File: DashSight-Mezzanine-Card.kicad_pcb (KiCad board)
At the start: 2 copper layers, 72 x 78.5 mm, 70 parts, among them IC1 XM1110, IC2 ELM327, J1 Pi2 Connector, J2 Euler Connector, J3 Conn_Coaxial, J4 OBD2-DB9_Male, Q1 2N3904, Q2 2N3906, Q3 2N3906, Q4 2N3904, Q5 2N3904, Q6 2N3904, Q7 2N3904, U1 MCP2561-E/P, U2 LM317L_TO92, U3 LM1085-5.0, U4 ADuM1201AR, Y1 4.0MHz

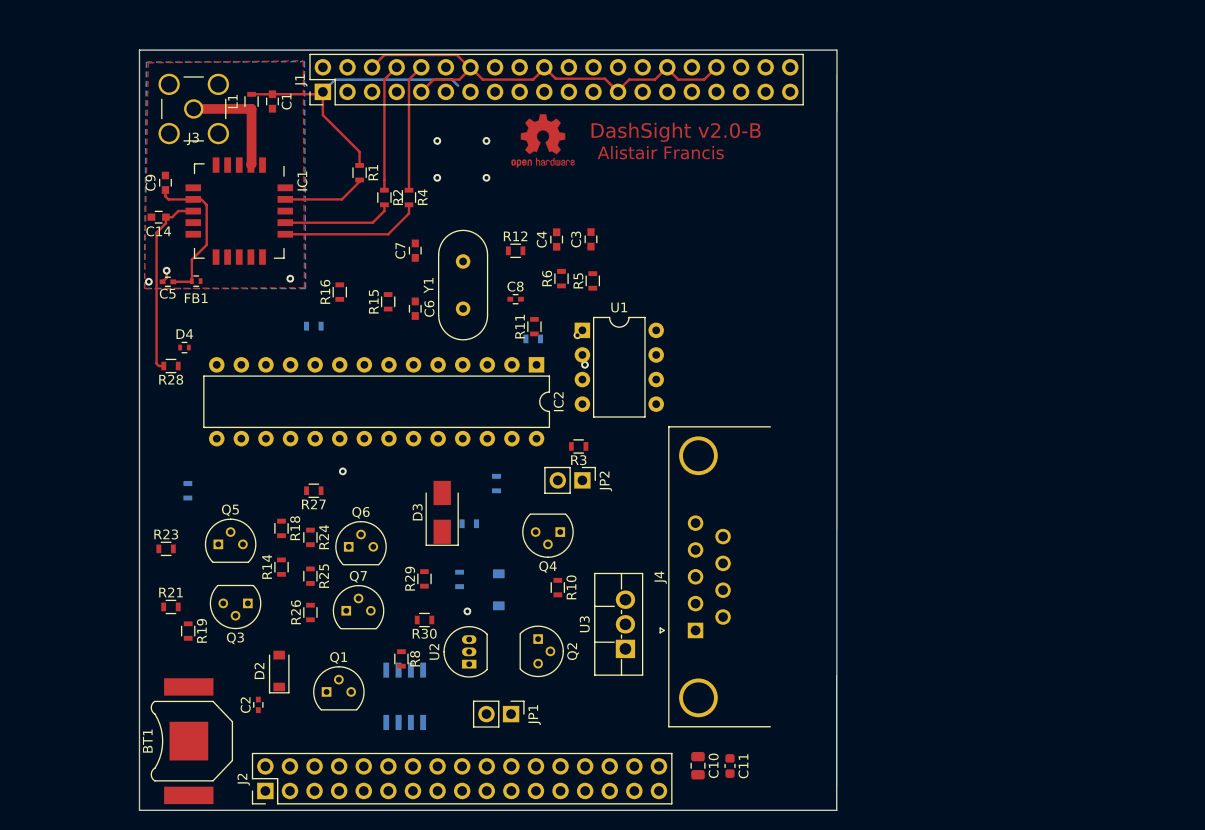
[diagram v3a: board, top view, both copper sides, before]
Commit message: pcb: Upgrade to 4 layers and start to prep GNSS
Signed-off-by: Alistair Francis <alistair@alistair23.me>
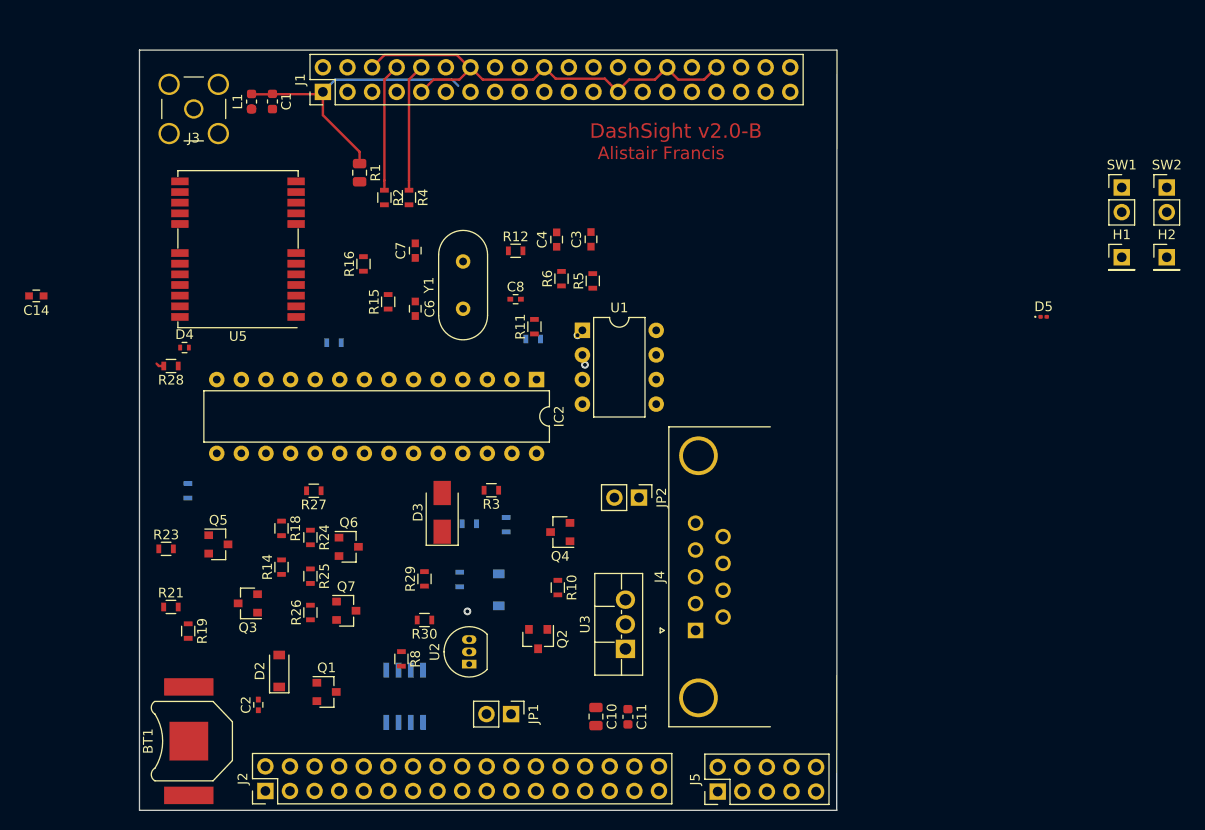
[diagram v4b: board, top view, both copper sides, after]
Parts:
- removed C5: 0.1uF, Capacitors_SMD:C_0402
- removed C9: 1uF, Capacitors_SMD:C_0603
- removed FB1: 600Ohm/100MHz, Inductors_SMD:L_0402
- removed IC1: XM1110, RF_GPS:Sierra_XM11X0
- removed REF***: OSHW-Logo2_7.3x6mm_Copper, Symbols:OSHW-Logo2_7.3x6mm_Copper
- added D5: D_Zener, Diode_SMD:D_0201_0603Metric, F.Cu at (221.4, 74.0)
- added H1: Safeboot, Connector_PinHeader_2.54mm:PinHeader_1x01_P2.54mm_Vertical, F.Cu at (229.4, 67.9)
- added H2: Reset, Connector_PinHeader_2.54mm:PinHeader_1x01_P2.54mm_Vertical, F.Cu at (234.1, 67.9)
- added J5: Conn_02x05_Odd_Even, Connector_PinHeader_2.54mm:PinHeader_2x05_P2.54mm_Vertical, F.Cu at (187.7, 123.1)
- added SW1: SW_Push, Connector_PinHeader_2.54mm:PinHeader_1x02_P2.54mm_Vertical, F.Cu at (229.4, 60.7)
- added SW2: SW_Push, Connector_PinHeader_2.54mm:PinHeader_1x02_P2.54mm_Vertical, F.Cu at (234.1, 60.7)
- added U5: NEO-M9N, RF_GPS:ublox_NEO, F.Cu at (138.2, 67.1)
- C1: value 1uF -> 47pF; footprint Capacitors_SMD:C_0603 -> Capacitor_SMD:C_0603_1608Metric
- L1: value 33nH -> 30Ohm/1.8A; footprint Inductors_SMD:L_0603 -> Inductor_SMD:L_0603_1608Metric
- Q1, Q2, Q3, Q4, Q5, Q6, Q7: footprint TO_SOT_Packages_THT:TO-92_Molded_Narrow -> Package_TO_SOT_SMD:SOT-23
- R1: value 10K -> 10; footprint Resistors_SMD:R_0603 -> Resistor_SMD:R_0805_2012Metric
- moved C14 15.0 mm to (117.3, 71.9)
- moved C10 11.7 mm to (175.1, 115.3)
- moved C11 11.7 mm to (178.4, 115.3)
- moved R3 10.1 mm to (164.3, 91.9)
- moved JP2 6.11 mm to (179.6, 92.7)
- moved R13 4.36 mm to (165.9, 95.5)
- moved R16 3.80 mm to (151.1, 68.6)
- moved R22 2.69 mm to (148.1, 76.7)
- moved IC2 1.52 mm to (169.0, 80.5)
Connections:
- C1 pad 1: +3V3 -> Net-(C1-Pad1)
- IC2 pad 25: Net-(IC2-Pad25) -> (no net)
- IC2 pad 26: Net-(IC2-Pad26) -> (no net)
- IC2 pad 27: Net-(IC2-Pad27) -> (no net)
- IC2 pad 28: Net-(IC2-Pad28) -> (no net)
- J1 pad 11: Net-(J1-Pad11) -> (no net)
- J1 pad 12: Net-(J1-Pad12) -> (no net)
- J1 pad 13: Net-(J1-Pad13) -> (no net)
- J1 pad 15: Net-(J1-Pad15) -> (no net)
- J1 pad 16: Net-(J1-Pad16) -> (no net)
- J1 pad 17: Net-(J1-Pad17) -> (no net)
- J1 pad 18: Net-(J1-Pad18) -> (no net)
- J1 pad 19: Net-(J1-Pad19) -> (no net)
- J1 pad 2: Net-(J1-Pad2) -> (no net)
- J1 pad 21: Net-(J1-Pad21) -> (no net)
- J1 pad 22: Net-(J1-Pad22) -> (no net)
- J1 pad 23: Net-(J1-Pad23) -> (no net)
- J1 pad 24: Net-(J1-Pad24) -> (no net)
- J1 pad 26: Net-(J1-Pad26) -> (no net)
- J1 pad 27: Net-(J1-Pad27) -> (no net)
- J1 pad 28: Net-(J1-Pad28) -> (no net)
- J1 pad 29: Net-(J1-Pad29) -> (no net)
- J1 pad 3: Net-(J1-Pad3) -> (no net)
- J1 pad 31: Net-(J1-Pad31) -> (no net)
- J1 pad 32: Net-(J1-Pad32) -> (no net)
- J1 pad 33: Net-(J1-Pad33) -> (no net)
- J1 pad 35: Net-(J1-Pad35) -> (no net)
- J1 pad 36: Net-(J1-Pad36) -> (no net)
- J1 pad 37: Net-(J1-Pad37) -> (no net)
- J1 pad 38: Net-(J1-Pad38) -> (no net)
- J1 pad 4: Net-(J1-Pad4) -> (no net)
- J1 pad 40: Net-(J1-Pad40) -> (no net)
- J1 pad 5: Net-(J1-Pad5) -> (no net)
- J1 pad 7: Net-(J1-Pad7) -> (no net)
- J2 pad 1: Net-(J2-Pad1) -> (no net)
- J2 pad 10: Net-(J2-Pad10) -> (no net)
- J2 pad 11: Net-(J2-Pad11) -> (no net)
- J2 pad 12: Net-(J2-Pad12) -> (no net)
- J2 pad 13: Net-(J2-Pad13) -> (no net)
- J2 pad 15: Net-(J2-Pad15) -> (no net)
- J2 pad 16: Net-(J2-Pad16) -> (no net)
- J2 pad 17: Net-(J2-Pad17) -> (no net)
- J2 pad 18: Net-(J2-Pad18) -> (no net)
- J2 pad 19: Net-(J2-Pad19) -> (no net)
- J2 pad 21: Net-(J2-Pad21) -> (no net)
- J2 pad 22: Net-(J2-Pad22) -> (no net)
- J2 pad 26: Net-(J2-Pad26) -> (no net)
- J2 pad 27: Net-(J2-Pad27) -> (no net)
- J2 pad 28: Net-(J2-Pad28) -> (no net)
- J2 pad 29: Net-(J2-Pad29) -> (no net)
- J2 pad 3: Net-(J2-Pad3) -> (no net)
- J2 pad 30: Net-(J2-Pad30) -> (no net)
- J2 pad 31: Net-(J2-Pad31) -> (no net)
- J2 pad 32: Net-(J2-Pad32) -> (no net)
- J2 pad 33: Net-(J2-Pad33) -> (no net)
- J2 pad 5: Net-(J2-Pad5) -> (no net)
- J2 pad 7: Net-(J2-Pad7) -> (no net)
- J2 pad 8: Net-(J2-Pad8) -> (no net)
- L1 pad 2: +3V3 -> Net-(C1-Pad1)
- R1 pad 1: +3V3 -> Net-(C1-Pad1)
- R2 pad 1: UART2_TX -> Net-(R2-Pad1)
- R2 pad 2: Net-(IC1-Pad17) -> UART2_TX
- R4 pad 1: UART2_RX -> Net-(R4-Pad1)
- R4 pad 2: Net-(IC1-Pad16) -> UART2_RX
- U1 pad 5: Net-(U1-Pad5) -> (no net)
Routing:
- net Net-(BT1-Pad1): track 19.5 -> 0.84 mm
- net Net-(C5-Pad1): track 16.7 -> 0.00 mm
- net Net-(IC1-Pad16): track 14.6 -> 0.00 mm
- net Net-(D5-Pad1): track 11.8 -> 0.02 mm
- net Net-(IC1-Pad17): track 11.4 -> 0.00 mm
- net Net-(R1-Pad2): track 8.62 -> 0.18 mm
- net GND: track 48.7 -> 47.3 mm, vias 7 -> 0
- net ELM_Pin12: vias 1 -> 0
- removed copper zone on B.Cu, net GND
- removed copper zone on F.Cu, net GND
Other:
- copper layers 2 -> 4

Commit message: pcb: Add ground and power planes on inner layers
Signed-off-by: Alistair Francis <alistair@alistair23.me>
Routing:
- added copper zone on In2.Cu, net +3V3
- added copper zone on In1.Cu, net GND
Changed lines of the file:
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@@
     (add_net "Net-(IC2-Pad21)")
     (add_net "Net-(IC2-Pad22)")
-    (add_net "Net-(IC2-Pad25)")
-    (add_net "Net-(IC2-Pad26)")
-    (add_net "Net-(IC2-Pad27)")
-    (add_net "Net-(IC2-Pad28)")
     (add_net "Net-(IC2-Pad3)")
     (add_net "Net-(IC2-Pad4)")
-    (add_net "Net-(J1-Pad11)")
-    (add_net "Net-(J1-Pad12)")
-    (add_net "Net-(J1-Pad13)")
-    (add_net "Net-(J1-Pad15)")
-    (add_net "Net-(J1-Pad16)")
-    (add_net "Net-(J1-Pad17)")
-    (add_net "Net-(J1-Pad18)")
-    (add_net "Net-(J1-Pad19)")
-    (add_net "Net-(J1-Pad2)")
-    (add_net "Net-(J1-Pad21)")
-    (add_net "Net-(J1-Pad22)")
-    (add_net "Net-(J1-Pad23)")
-    (add_net "Net-(J1-Pad24)")
-    (add_net "Net-(J1-Pad26)")
-    (add_net "Net-(J1-Pad27)")
-    (add_net "Net-(J1-Pad28)")
-    (add_net "Net-(J1-Pad29)")
-    (add_net "Net-(J1-Pad3)")
-    (add_net "Net-(J1-Pad31)")
-    (add_net "Net-(J1-Pad32)")
-    (add_net "Net-(J1-Pad33)")
-    (add_net "Net-(J1-Pad35)")
-    (add_net "Net-(J1-Pad36)")
-    (add_net "Net-(J1-Pad37)")
-    (add_net "Net-(J1-Pad38)")
-    (add_net "Net-(J1-Pad4)")
-    (add_net "Net-(J1-Pad40)")
-    (add_net "Net-(J1-Pad5)")
-    (add_net "Net-(J1-Pad7)")
-    (add_net "Net-(J2-Pad1)")
-    (add_net "Net-(J2-Pad10)")
-    (add_net "Net-(J2-Pad11)")
-    (add_net "Net-(J2-Pad12)")
-    (add_net "Net-(J2-Pad13)")
-    (add_net "Net-(J2-Pad15)")
-    (add_net "Net-(J2-Pad16)")
-    (add_net "Net-(J2-Pad17)")
-    (add_net "Net-(J2-Pad18)")
-    (add_net "Net-(J2-Pad19)")
-    (add_net "Net-(J2-Pad21)")
-    (add_net "Net-(J2-Pad22)")
-    (add_net "Net-(J2-Pad26)")
-    (add_net "Net-(J2-Pad27)")
-    (add_net "Net-(J2-Pad28)")
-    (add_net "Net-(J2-Pad29)")
-    (add_net "Net-(J2-Pad3)")
-    (add_net "Net-(J2-Pad30)")
-    (add_net "Net-(J2-Pad31)")
-    (add_net "Net-(J2-Pad32)")
-    (add_net "Net-(J2-Pad33)")
-    (add_net "Net-(J2-Pad5)")
-    (add_net "Net-(J2-Pad7)")
-    (add_net "Net-(J2-Pad8)")
-    (add_net "Net-(J5-Pad10)")
-    (add_net "Net-(J5-Pad2)")
-    (add_net "Net-(J5-Pad3)")
-    (add_net "Net-(J5-Pad7)")
-    (add_net "Net-(J5-Pad8)")
     (add_net "Net-(Q1-Pad2)")
     (add_net "Net-(Q2-Pad1)")
@@
     (add_net "Net-(R3-Pad1)")
     (add_net "Net-(R4-Pad1)")
-    (add_net "Net-(U1-Pad5)")
-    (add_net "Net-(U5-Pad14)")
-    (add_net "Net-(U5-Pad15)")
-    (add_net "Net-(U5-Pad16)")
-    (add_net "Net-(U5-Pad17)")
-    (add_net "Net-(U5-Pad18)")
-    (add_net "Net-(U5-Pad19)")
-    (add_net "Net-(U5-Pad3)")
-    (add_net "Net-(U5-Pad4)")
-    (add_net "Net-(U5-Pad5)")
-    (add_net "Net-(U5-Pad6)")
     (add_net PowerOn)
     (add_net PwrCntrl)
-    (add_net ResetSW)
     (add_net UART2_RX)
     (add_net UART2_TX)
@@
   (segment (start 155.829 59.956) (end 155.829 49.53) (width 0.25) (layer F.Cu) (net 19))
   (segment (start 155.829 60.972) (end 155.829 59.956) (width 0.25) (layer F.Cu) (net 19))
+  (segment (start 155.829 62.472) (end 155.829 62.484) (width 0.25) (layer F.Cu) (net 19) (status 30))
   (via (at 174 79) (size 0.8) (drill 0.4) (layers F.Cu B.Cu) (net 27))
   (segment (start 160.909 50.181) (end 160.274 49.546) (width 0.25) (layer B.Cu) (net 35))
@@
   (segment (start 153.289 60.972) (end 153.289 59.956) (width 0.25) (layer F.Cu) (net 38))
   (via (at 173.228 75.946) (size 0.8) (drill 0.4) (layers F.Cu B.Cu) (net 42))
-  (segment (start 155.829 62.472) (end 155.829 62.484) (width 0.25) (layer F.Cu) (net 19) (status 30))
-  (segment (start 150.731 59.909) (end 150.731 60.089) (width 0.25) (layer F.Cu) (net 57) (status 30))
   (segment (start 129.761999 78.878499) (end 130.0045 79.121) (width 0.25) (layer F.Cu) (net 45))
   (segment (start 130.0045 79.121) (end 130.5045 79.121) (width 0.25) (layer F.Cu) (net 45))
   (segment (start 139.561 52.578) (end 139.573 52.566) (width 1) (layer F.Cu) (net 53))
+  (segment (start 150.731 59.909) (end 150.731 60.089) (width 0.25) (layer F.Cu) (net 57) (status 30))
+  (zone (net 1) (net_name GND) (layer In1.Cu) (hatch edge 0.508)
+    (connect_pads (clearance 0.508))
+    (min_thickness 0.254)
+    (fill yes (arc_segments 32) (thermal_gap 0.508) (thermal_bridge_width 0.508))
+    (polygon
+      (pts
+        (xy 199.39 123.825) (xy 128.905 123.825) (xy 128.905 47.625) (xy 199.39 47.625)
+      )
+    )
+  )
+  (zone (net 35) (net_name +3V3) (layer In2.Cu) (hatch edge 0.508)
+    (connect_pads (clearance 0.508))
+    (min_thickness 0.254)
+    (fill yes (arc_segments 32) (thermal_gap 0.508) (thermal_bridge_width 0.508))
+    (polygon
+      (pts
+        (xy 196.85 118.11) (xy 130.81 118.11) (xy 130.81 53.34) (xy 196.85 53.34)
+      )
+    )
+  )
 )

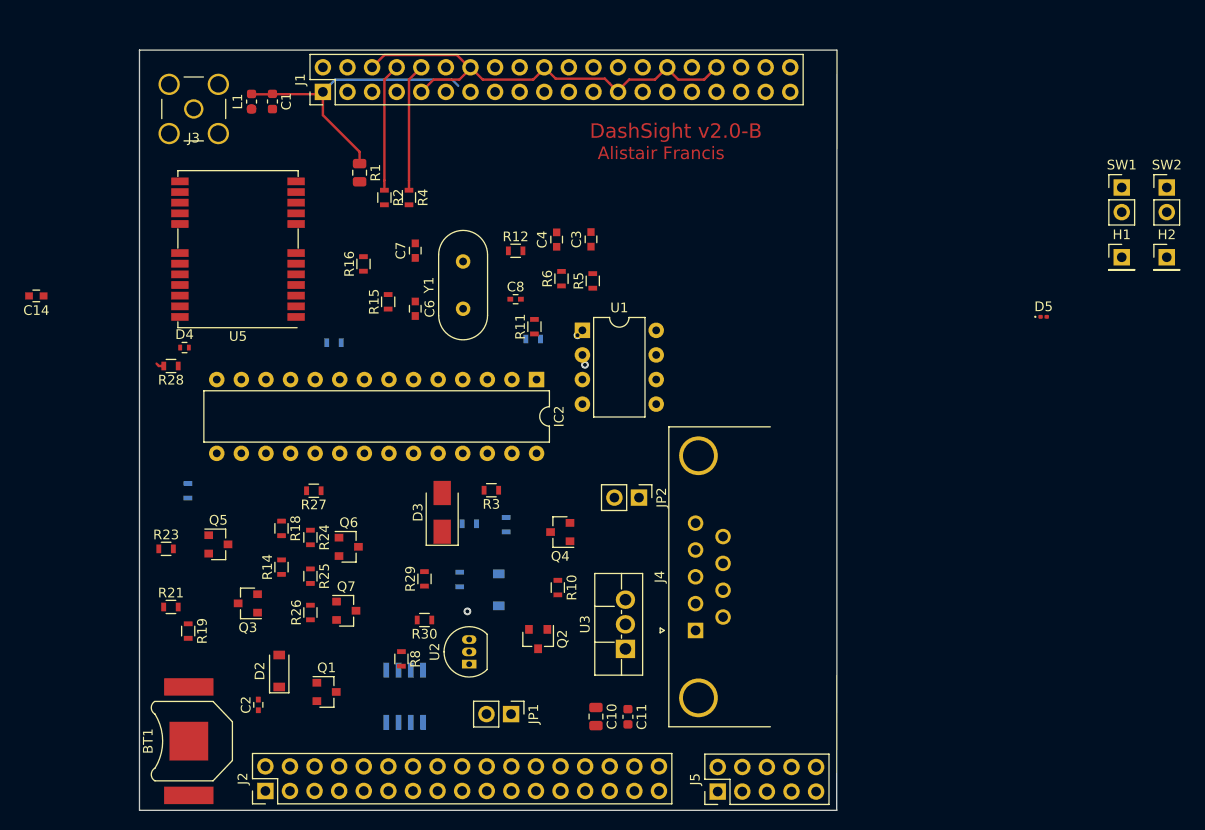
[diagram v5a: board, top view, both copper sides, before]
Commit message: pcb: Start to connect up the GNSS receiver
Signed-off-by: Alistair Francis <alistair@alistair23.me>
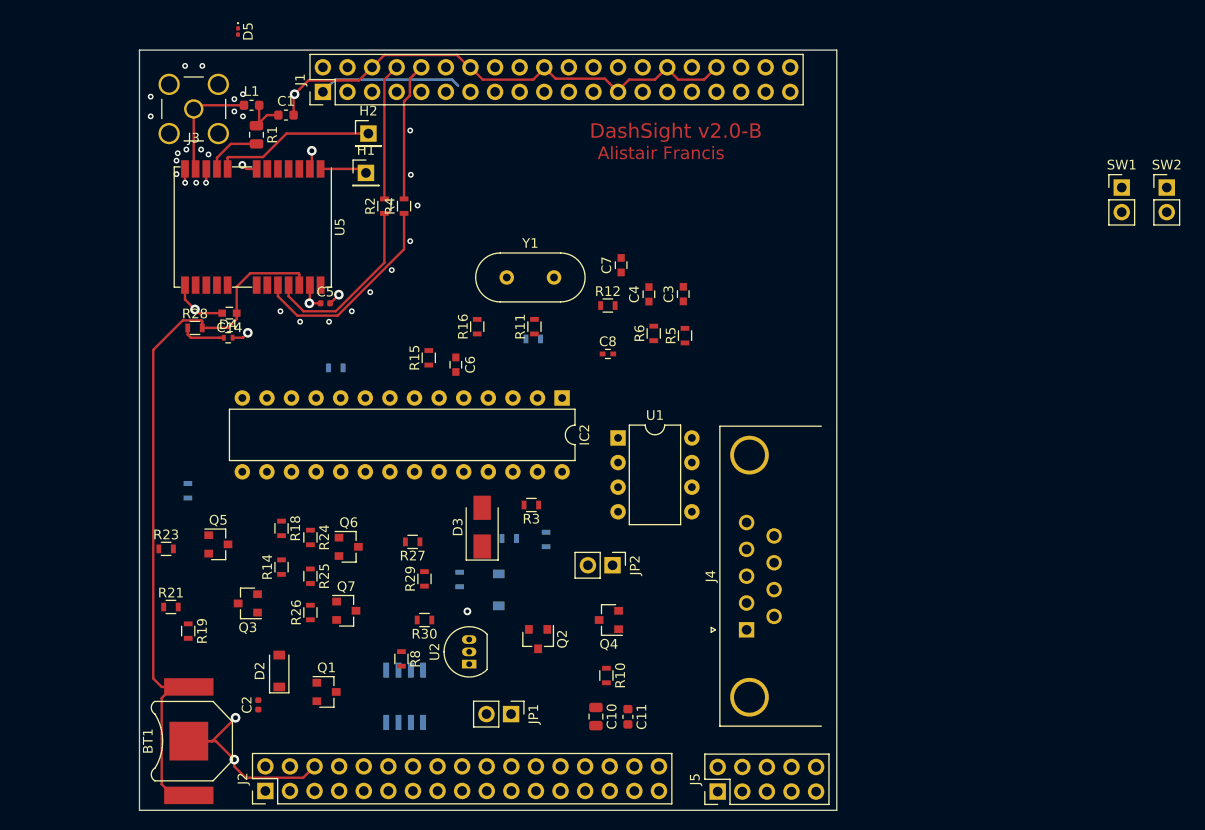
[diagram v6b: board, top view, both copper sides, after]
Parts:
- removed U3: LM1085-5.0, Package_TO_SOT_THT:TO-220F-3_Vertical
- added C5: 0.1uF, Capacitor_SMD:C_0402_1005Metric, F.Cu at (147.2, 72.6)
- C2: footprint Capacitors_SMD:C_0402 -> Capacitor_SMD:C_0402_1005Metric
- moved D5 88.2 mm to (138.2, 44.6), turned to 270 degrees
- moved H2 83.4 mm to (151.6, 55.1)
- moved H1 78.5 mm to (151.4, 59.2)
- moved C7 21.3 mm to (177.7, 68.7)
- moved C14 20.0 mm to (137.3, 73.7)
- moved R16 13.4 mm to (162.9, 75.1)
- moved U1 11.7 mm to (177.4, 86.6)
- moved R27 11.5 mm to (156.2, 97.3)
- moved R1 11.3 mm to (140.1, 55.2)
- moved C4 11.1 mm to (180.6, 71.7)
- moved C3 11.1 mm to (184.2, 71.7)
- moved C8 11.1 mm to (176.4, 77.9)
- moved R12 11.1 mm to (176.4, 72.9)
- moved R5 11.1 mm to (184.3, 76.0)
- moved R6 11.1 mm to (181.1, 75.8)
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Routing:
- net Net-(BT1-Pad1): track 0.84 -> 76.0 mm
- net GND: track 47.3 -> 85.6 mm, vias 0 -> 33
- net Net-(R4-Pad1): track 0.00 -> 21.5 mm
- net Net-(R2-Pad1): track 0.00 -> 18.9 mm
- net Net-(H2-Pad1): track 0.00 -> 16.7 mm
- net Net-(D5-Pad1): track 0.02 -> 11.6 mm
- net +3V3: track 31.4 -> 21.9 mm, vias 0 -> 3
- net Net-(R1-Pad2): track 0.18 -> 5.83 mm
- net Net-(C1-Pad1): track 0.00 -> 4.94 mm
- net Net-(H1-Pad1): track 0.00 -> 4.85 mm
- net Net-(D4-Pad1): track 0.00 -> 4.56 mm
- net UART2_RX: track 13.3 -> 14.3 mm
- net UART2_TX: track 13.6 -> 14.5 mm
- net Net-(R13-Pad2): vias 1 -> 0
- net CAN_TX: vias 1 -> 0
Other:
- net class RF: trace_width 1 -> 0.2
